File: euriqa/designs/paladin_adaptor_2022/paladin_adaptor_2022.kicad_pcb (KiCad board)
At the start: 2 copper layers, 33.7 x 52.1 mm, 3 parts, among them J1 Conn_02x15_Odd_Even, J2 Conn_02x15_Odd_Even, U1 Conn_03x20

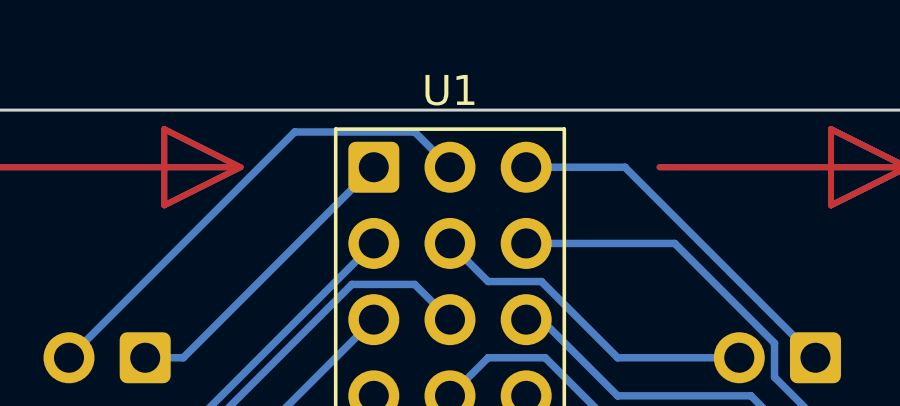
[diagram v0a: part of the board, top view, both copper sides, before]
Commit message: [euriqa/designs/paladin_adaptor_2022] Relative path, update prefix letter
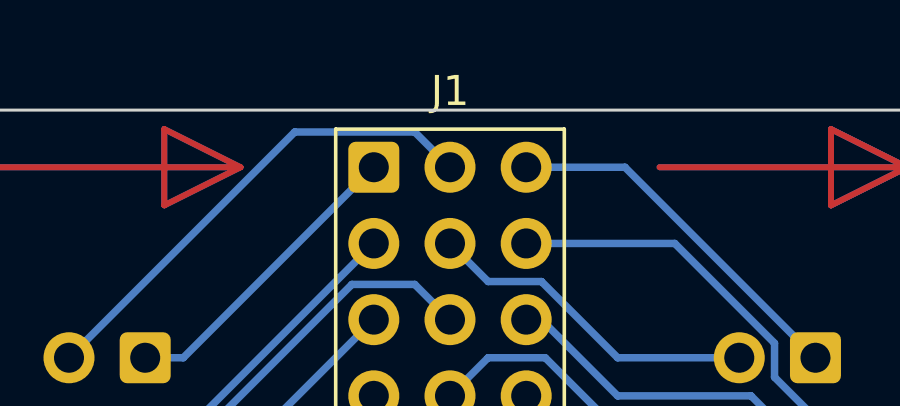
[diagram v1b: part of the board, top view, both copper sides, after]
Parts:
- renumbered U1 to J1, J1 to J2, J2 to J3
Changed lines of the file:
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@@
     (property "Sheetname" "")
     (attr through_hole)
-    (fp_text reference "U1" (at 2.54 -2.54) (layer "F.SilkS")
+    (fp_text reference "J1" (at 2.54 -2.54) (layer "F.SilkS")
       (effects (font (size 1 1) (thickness 0.15)))
     )
@@
     (property "Sheetname" "")
     (attr through_hole)
-    (fp_text reference "J2" (at 7.1025 5.08) (layer "B.SilkS")
+    (fp_text reference "J3" (at 7.1025 5.08) (layer "B.SilkS")
       (effects (font (size 1 1) (thickness 0.15)) (justify mirror))
     )
@@
     (property "Sheetname" "")
     (attr through_hole)
-    (fp_text reference "J1" (at -4.445 5.08) (layer "B.SilkS")
-      (effects (font (size 1 1) (thickness 0.15)) (justify mirror))
-    )
+    (fp_text reference "J2" (at -4.445 5.08) (layer "B.SilkS")
+      (effects (font (size 1 1) (thickness 0.15)) (justify mirror))
+    )

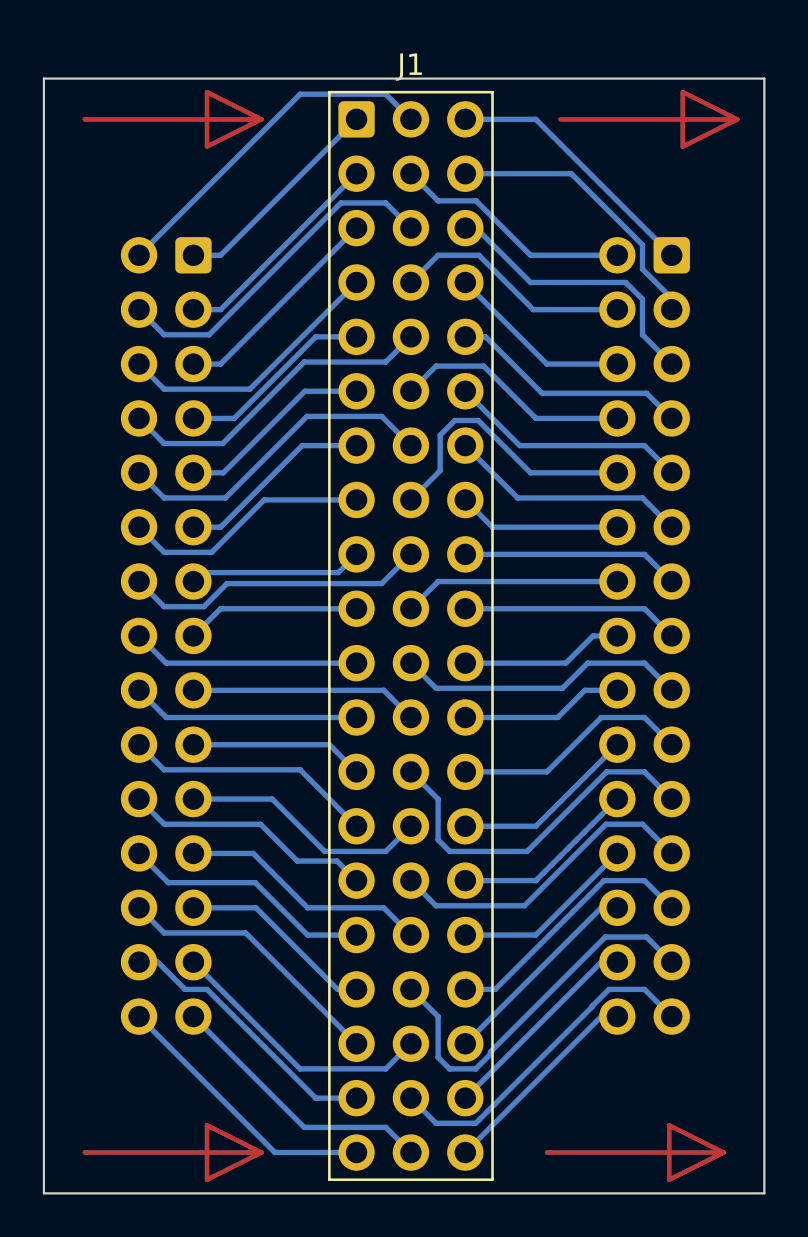
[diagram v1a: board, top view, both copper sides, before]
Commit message: [euriqa/designs/paladin_adaptor_2022] Reduce board size
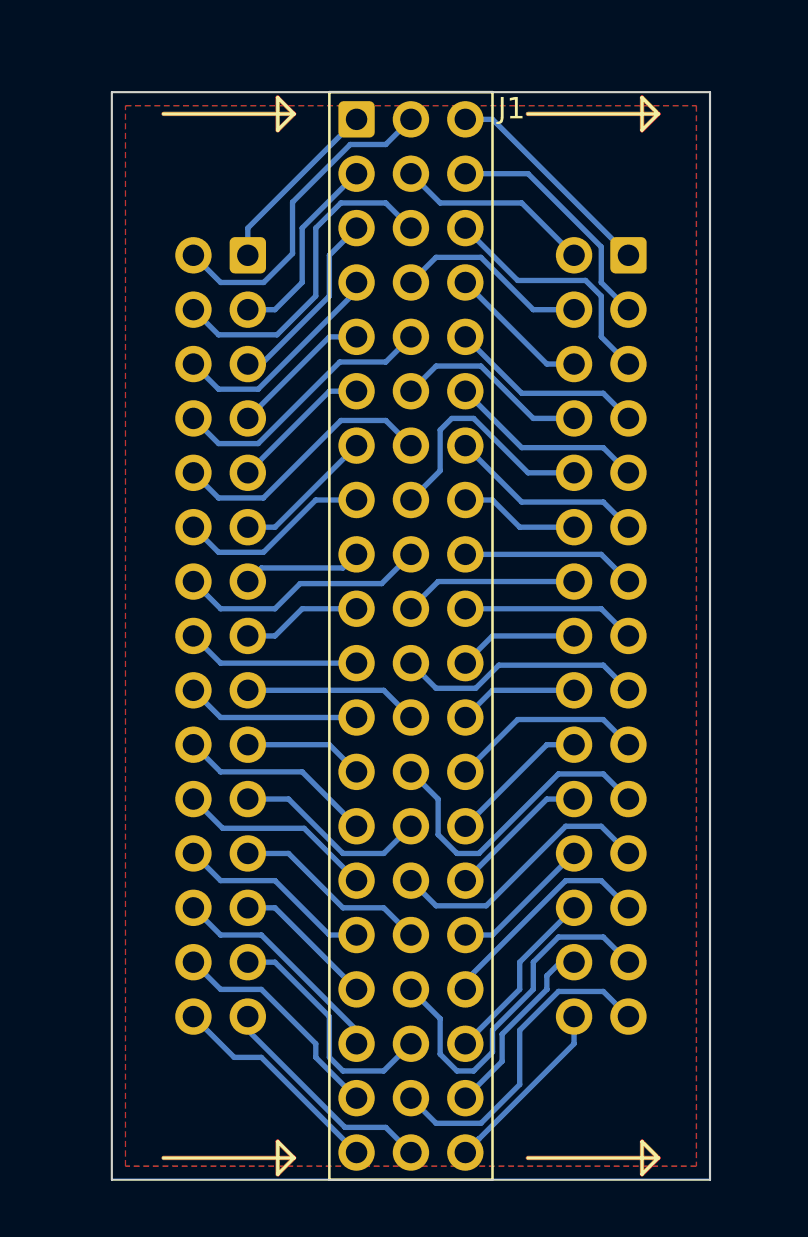
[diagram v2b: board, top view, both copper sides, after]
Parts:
- moved J2 2.54 mm to (102.9, 58.4)
- moved J3 2.02 mm to (120.7, 58.4)
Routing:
- net P27: track 15.3 -> 12.6 mm
- net P17: track 9.20 -> 6.66 mm
- net P7: track 9.20 -> 6.66 mm
- net P6: track 9.20 -> 6.66 mm
- net P32: track 10.7 -> 8.15 mm
- net P13: track 8.15 -> 5.61 mm
- net P10: track 8.15 -> 5.61 mm
- net P9: track 8.15 -> 5.61 mm
- net P36: track 11.7 -> 9.20 mm
- net P25: track 15.3 -> 12.7 mm
- net P20: track 12.8 -> 10.3 mm
- net P16: track 11.7 -> 9.20 mm
- net P14: track 11.7 -> 9.20 mm
- net P12: track 10.7 -> 8.15 mm
- net P11: track 10.7 -> 8.15 mm
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- added copper zone on F.Cu, net (none)
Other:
- board size 33.7 x 52.1 mm -> 27.9 x 50.8 mm
